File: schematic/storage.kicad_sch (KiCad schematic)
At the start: 7 parts, among them U2 27C256, U3 SCM2114AL, U4 SCM2114AL

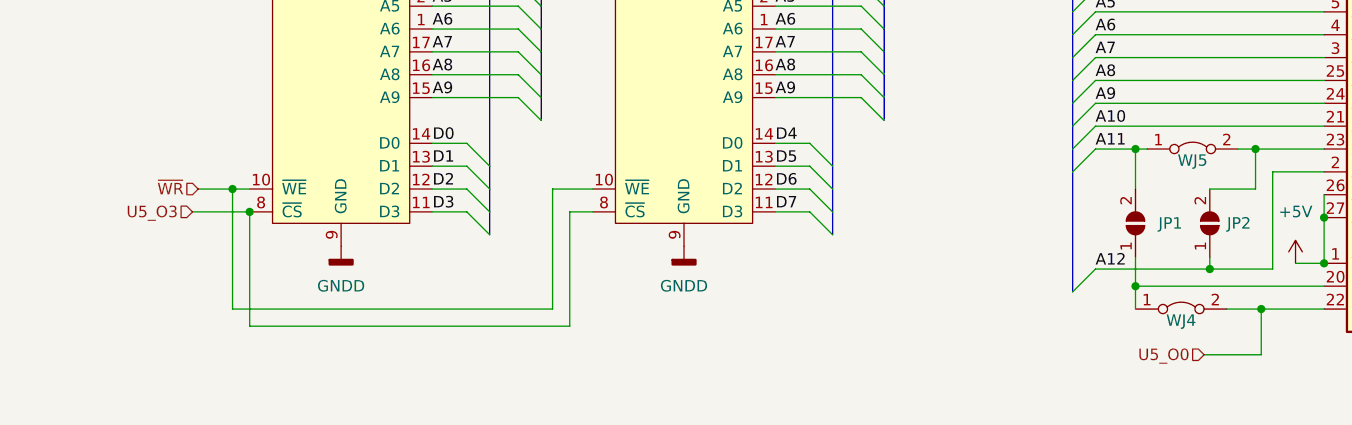
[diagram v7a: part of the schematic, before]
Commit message: added u6 decoder lines, renamed a few lines to make sense to there destination.
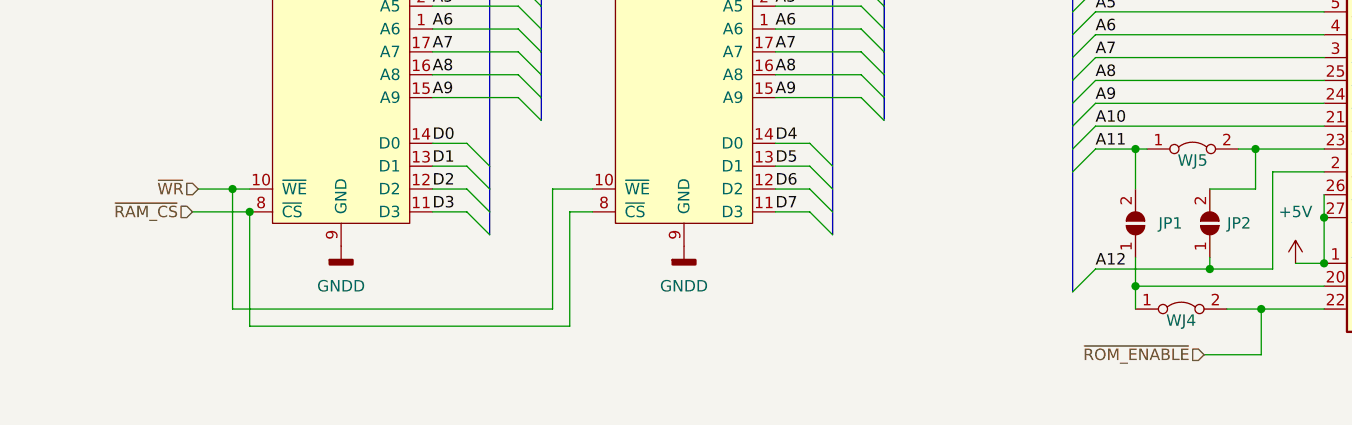
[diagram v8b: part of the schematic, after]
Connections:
- net U5_O0 renamed ~{ROM_ENABLE}
- net U5_O3 renamed ~{RAM_CS}
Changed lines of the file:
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@@
     (effects (font (size 1.27 1.27)) (justify left bottom))
   )
-  (hierarchical_label "U5_O0" (shape input) (at 193.04 126.365 180)
+  (hierarchical_label "~{ROM_ENABLE}" (shape input) (at 193.04 126.365 180)
     (effects (font (size 1.27 1.27)) (justify right))
   )
@@
     (effects (font (size 1.27 1.27)) (justify right))
   )
-  (hierarchical_label "U5_O3" (shape input) (at 80.645 110.49 180)
+  (hierarchical_label "~{RAM_CS}" (shape input) (at 80.645 110.49 180)
     (effects (font (size 1.27 1.27)) (justify right))
   )
